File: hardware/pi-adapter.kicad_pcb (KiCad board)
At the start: 2 copper layers, 64 x 56 mm, 36 parts, among them P1 CONN_02X20, P10 CONN_01X04, P100 CONN_01X01, P101 CONN_01X01, P103 CONN_01X01, P11 CONN_01X04, P12 CONN_01X04, P13 CONN_01X04, P14 CONN_01X04, P15 CONN_01X04, P16 CONN_01X04, P17 CONN_01X04, P18 CONN_01X04, P19 CONN_01X04, P2 +5V, P20 CONN_01X04, P21 CONN_01X04, P3 CONN_01X03, P4 GND, P5 CONN_01X03, P6 CONN_01X04, P7 CONN_01X04, P8 CONN_01X04, P9 CONN_01X04, U1 74HCT245, U2 74HCT245, U3 74HCT245, U4 74HCT245

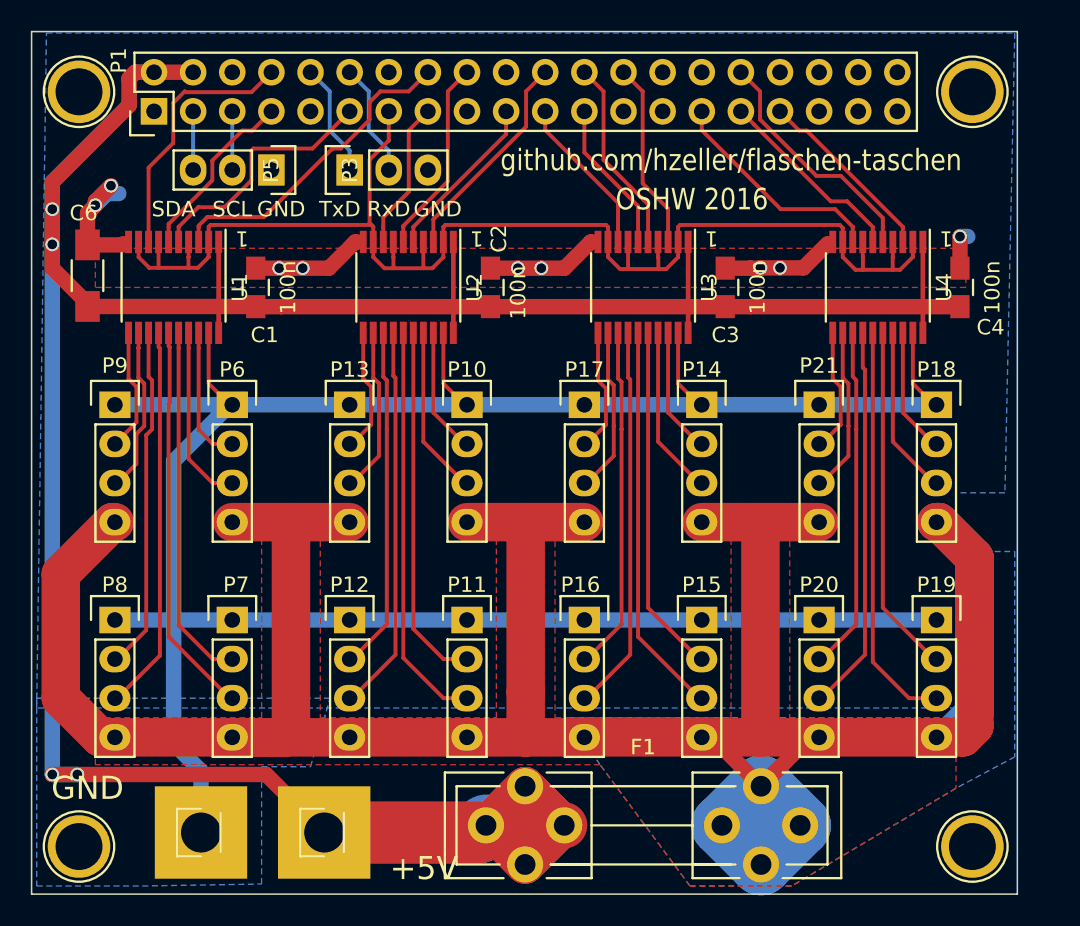
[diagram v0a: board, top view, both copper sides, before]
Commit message: o Break out SPI bus as well.
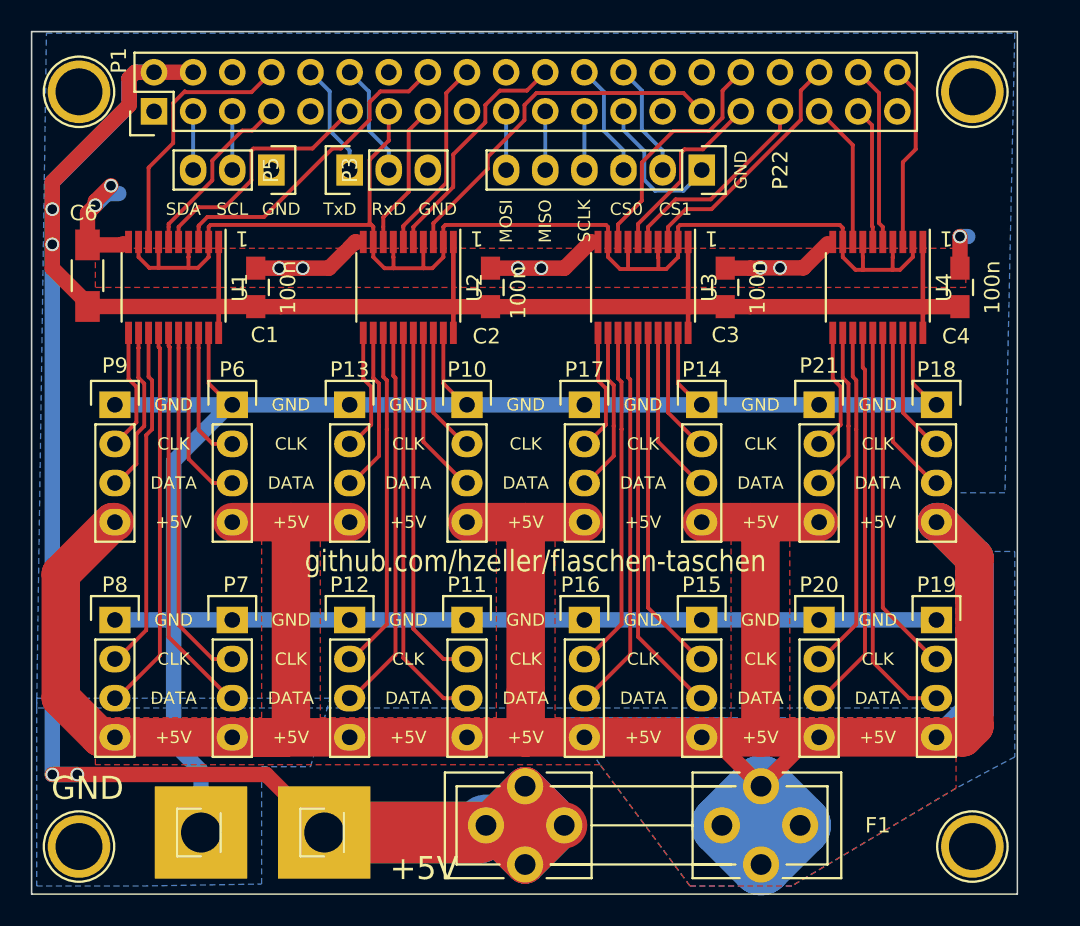
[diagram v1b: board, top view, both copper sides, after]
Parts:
- added P22: CONN_01X06, Pin_Headers:Pin_Header_Straight_1x06, F.Cu at (143.5, 47.0)
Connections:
- P1 pad 19: D6 -> /MOSI
- P1 pad 21: D9 -> /MISO
- P1 pad 22: D8 -> D6
- P1 pad 23: D11 -> /SCLK
- P1 pad 24: D10 -> CS0
- P1 pad 26: D12 -> CS1
- P1 pad 29: D13 -> D8
- P1 pad 31: D14 -> D11
- P1 pad 32: D15 -> D9
- P1 pad 33: D16 -> D10
- P1 pad 35: (no net) -> D13
- P1 pad 36: (no net) -> D12
- P1 pad 37: (no net) -> D14
- P1 pad 38: (no net) -> D15
- P1 pad 40: (no net) -> D16
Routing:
- net GND: track 193.5 -> 203.2 mm
- net D8: track 14.0 -> 23.7 mm
- net CS0: track 0.00 -> 7.40 mm
- net CS1: track 0.00 -> 7.40 mm
- net D9: track 10.4 -> 15.7 mm
- net D13: track 14.6 -> 9.39 mm
- net D6: track 11.0 -> 15.6 mm
- net D15: track 15.8 -> 11.7 mm
- net D12: track 12.2 -> 16.1 mm
- net /SCLK: track 0.00 -> 3.81 mm
- net /MOSI: track 0.00 -> 3.81 mm
- net /MISO: track 0.00 -> 3.81 mm
- net D14: track 12.7 -> 8.87 mm
- net D11: track 9.92 -> 11.9 mm
- net D10: track 12.7 -> 13.4 mm
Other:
- board text added: "CLK"
- board text added: "CS0"
- board text added: "CS1"
- board text added: "DATA"
- board text added: "MISO"
- board text added: "MOSI"
- board text added: "SCLK"
- board text removed: "OSHW 2016"

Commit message: o Better sequential labelling of data lines. o Improve higher current traces.
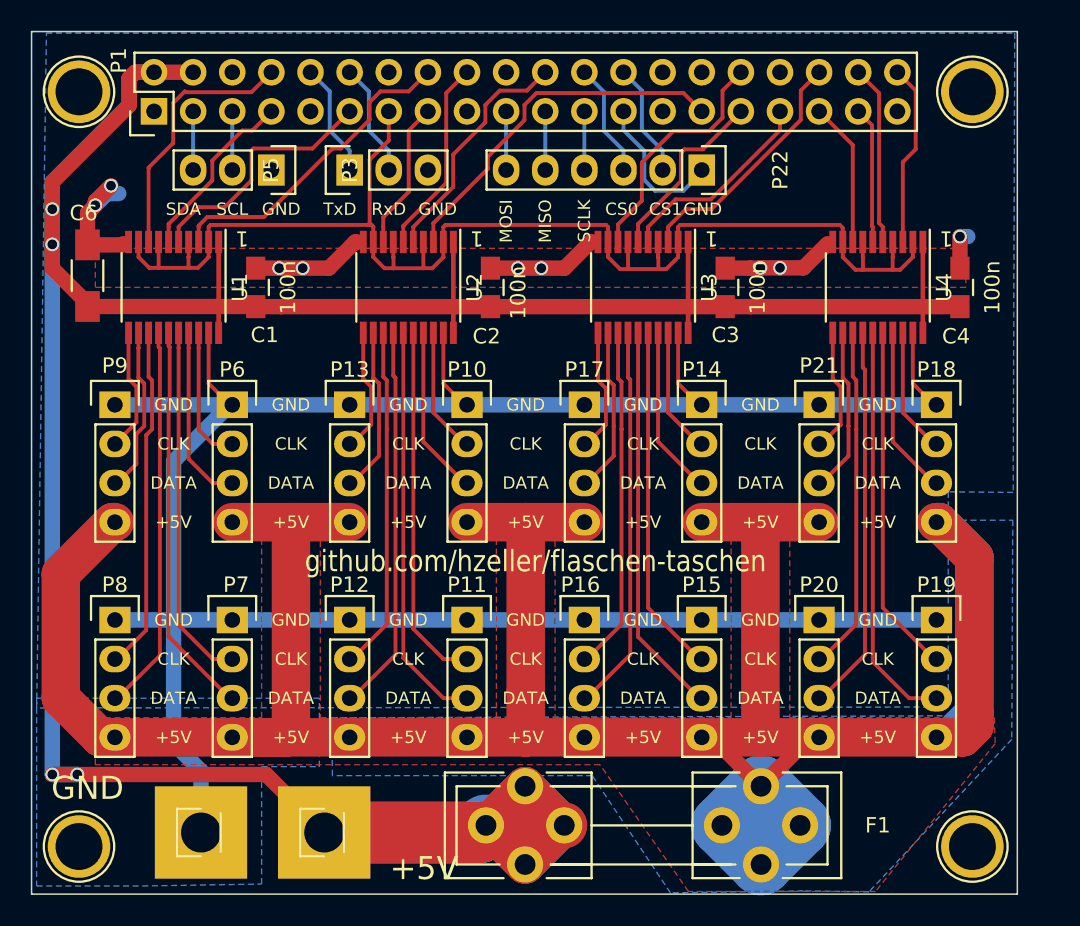
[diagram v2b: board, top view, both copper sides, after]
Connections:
- P1 pad 18: D7 -> D6
- P1 pad 22: D6 -> D7
- P1 pad 31: D11 -> D10
- P1 pad 33: D10 -> D11
- U2 pad 5: D6 -> D7
- U2 pad 6: D7 -> D6
- U3 pad 5: D10 -> D11
- U3 pad 6: D11 -> D10
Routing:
- net D7: track 12.7 -> 15.6 mm
- net D6: track 15.6 -> 12.7 mm
- net D11: track 11.9 -> 13.4 mm
- net D10: track 13.4 -> 11.9 mm

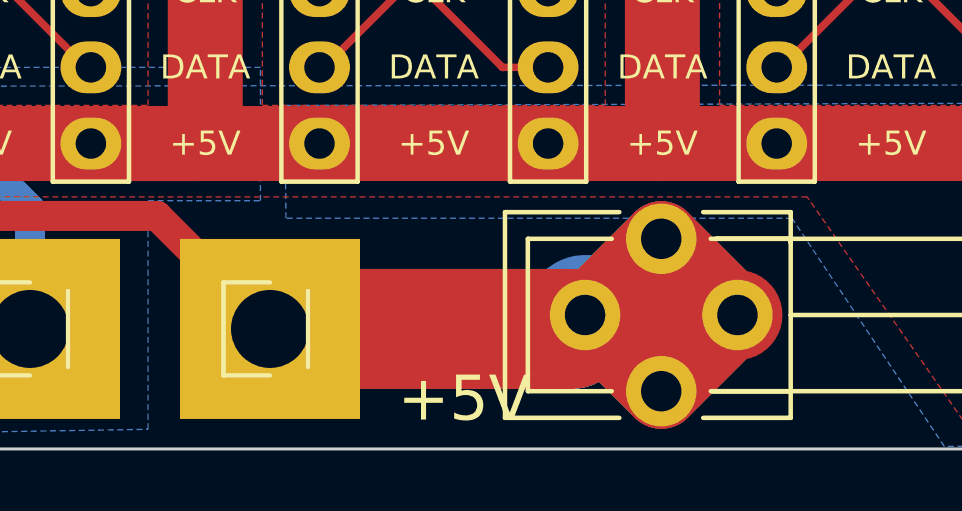
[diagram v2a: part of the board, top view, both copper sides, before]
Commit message: o Bit wider power input.
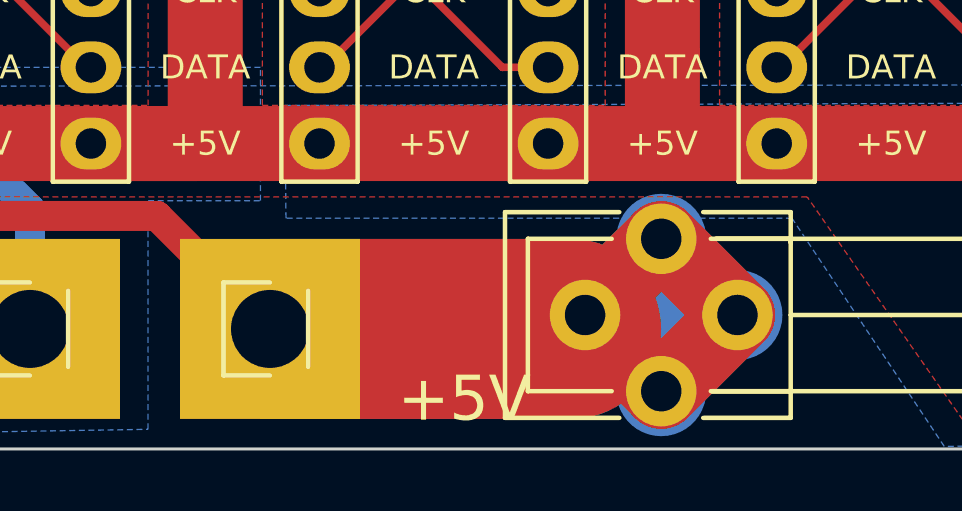
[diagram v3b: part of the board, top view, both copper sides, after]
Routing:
- net VCC: track 227.2 -> 232.3 mm
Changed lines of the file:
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@@
     (links 150)
     (no_connects 0)
-    (area 97.971667 37.949999 166.188334 96.86)
+    (area 99.949999 37.949999 164.050001 94.050001)
     (thickness 1.6)
     (drawings 80)
-    (tracks 538)
+    (tracks 539)
     (zones 0)
     (modules 37)
@@
   )
   (setup
-    (last_trace_width 0.254)
+    (last_trace_width 3)
     (user_trace_width 0.254)
     (user_trace_width 0.3048)
@@
   (gr_line (start 164 38) (end 164 94) (angle 90) (layer Edge.Cuts) (width 0.1))
   (gr_line (start 164 94) (end 100 94) (angle 90) (layer Edge.Cuts) (width 0.1))
+  (segment (start 132.0419 86.995) (end 132.0419 92.075) (width 3) (layer B.Cu) (net 1))
+  (segment (start 129.5019 89.535) (end 134.5819 89.535) (width 3) (layer B.Cu) (net 1))
   (segment (start 132.0419 86.995) (end 129.5019 89.535) (width 2.5) (layer B.Cu) (net 1))
   (segment (start 134.5819 89.535) (end 132.0419 86.995) (width 2.5) (layer B.Cu) (net 1))
@@
   (segment (start 132.0419 86.995) (end 134.5819 89.535) (width 2.5) (layer F.Cu) (net 1))
   (segment (start 129.5019 89.535) (end 132.0419 86.995) (width 2.5) (layer F.Cu) (net 1))
-  (segment (start 119 90) (end 129.0369 90) (width 4) (layer B.Cu) (net 1))
+  (segment (start 119 90) (end 129.0369 90) (width 6) (layer B.Cu) (net 1))
   (segment (start 129.0369 90) (end 129.5019 89.535) (width 4) (layer B.Cu) (net 1))
   (segment (start 101.346 53.362) (end 101.346 51.816) (width 1) (layer F.Cu) (net 1))
@@
   (segment (start 115.233 86.233) (end 101.346 86.233) (width 1) (layer F.Cu) (net 1))
   (via (at 101.346 86.233) (size 0.889) (drill 0.635) (layers F.Cu B.Cu) (net 1))
-  (segment (start 134.5819 89.535) (end 129.5019 89.535) (width 3) (layer F.Cu) (net 1))
-  (segment (start 119 90) (end 129.0369 90) (width 4) (layer F.Cu) (net 1))
+  (segment (start 119 90) (end 129.0369 90) (width 6) (layer F.Cu) (net 1))
   (segment (start 138.43 43.18) (end 138.43 44.401314) (width 0.254) (layer B.Cu) (net 2))
   (segment (start 138.43 44.401314) (end 139.77939 45.750704) (width 0.254) (layer B.Cu) (net 2))
